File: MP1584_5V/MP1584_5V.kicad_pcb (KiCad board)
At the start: 2 copper layers, 25 x 20 mm, 17 parts, among them J1 Conn_01x03_Pin

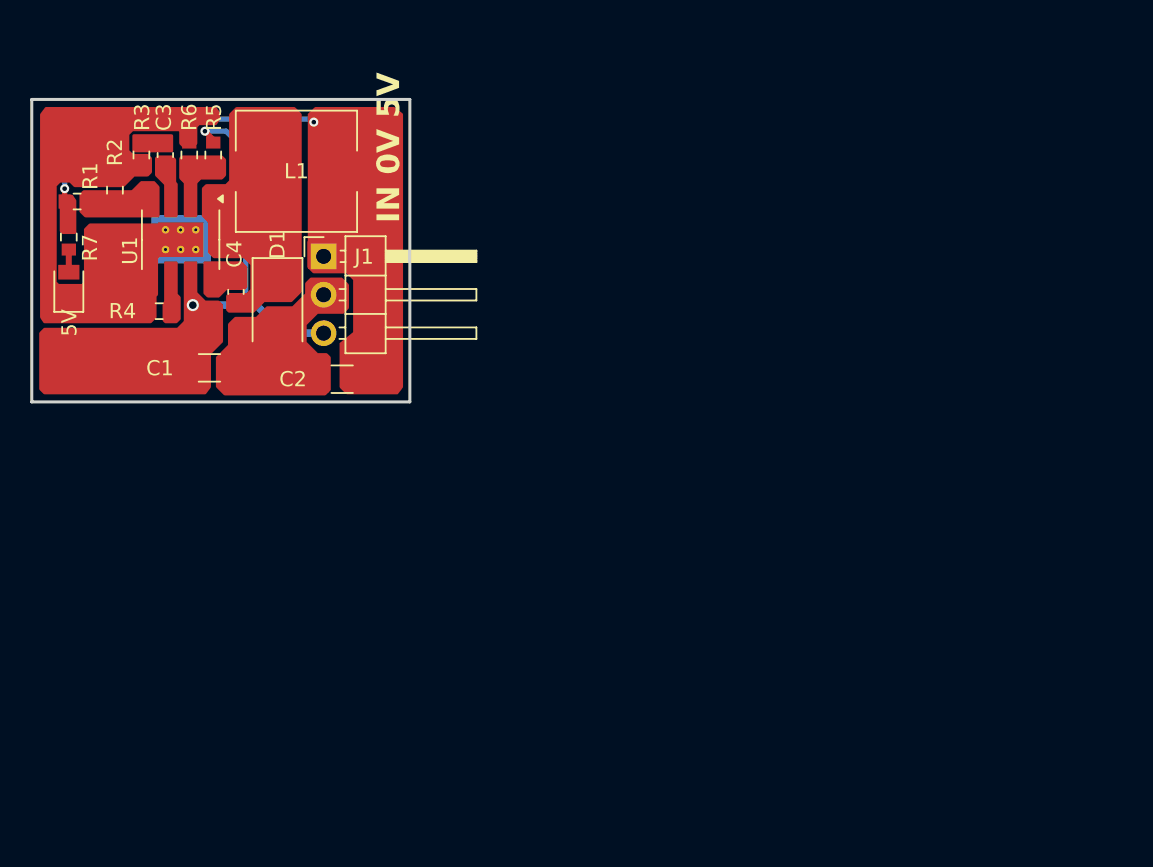
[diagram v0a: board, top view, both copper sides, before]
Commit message: Change to curved line trace.
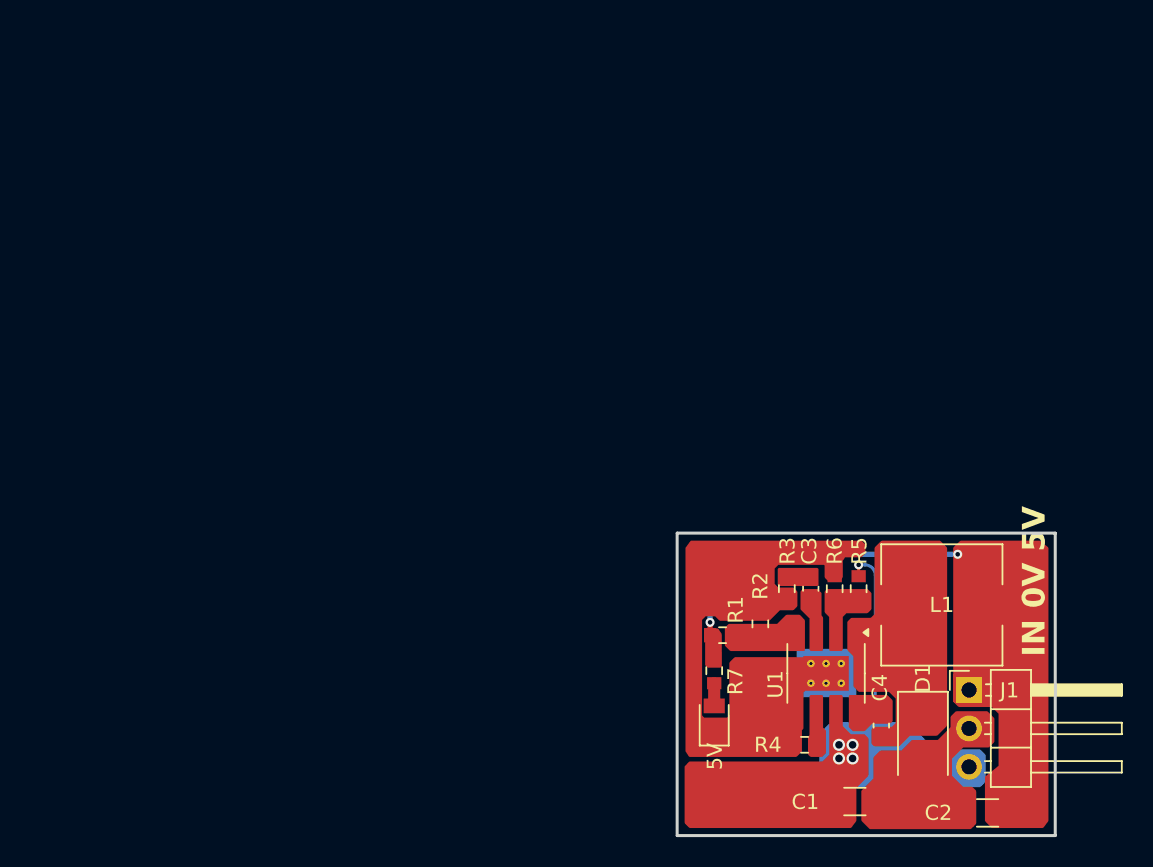
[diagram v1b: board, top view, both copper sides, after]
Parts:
- moved R7 51.4 mm to (121.9, 102.8)
- moved C1 51.4 mm to (131.2, 111.4)
- moved C3 51.4 mm to (128.2, 97.3)
- moved D1 51.4 mm to (135.7, 107.7)
- moved L1 51.4 mm to (136.9, 98.4)
- moved R5 51.4 mm to (131.4, 97.3)
- moved U1 51.4 mm to (129.3, 103.0)
- moved C4 51.4 mm to (132.9, 106.4)
- moved D2 51.4 mm to (121.9, 106.0)
- moved J1 51.4 mm to (138.7, 104.0)
- moved R1 51.4 mm to (122.4, 100.4)
- moved R2 51.4 mm to (124.9, 99.7)
- moved R3 51.4 mm to (126.7, 97.3)
- moved R4 51.4 mm to (127.8, 107.7)
- moved R6 51.4 mm to (129.8, 97.3)
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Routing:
- net VCC: track 23.8 -> 13.6 mm, vias 2 -> 5
- net +5V: track 20.6 -> 21.1 mm
